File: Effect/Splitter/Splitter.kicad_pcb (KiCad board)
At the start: 2 copper layers, 32 x 68.5 mm, 9 parts, among them J1 Conn_01x04_Pin, J2 AudioJack2_Ground, J3 Conn_01x03_Pin, U1 OPA1655

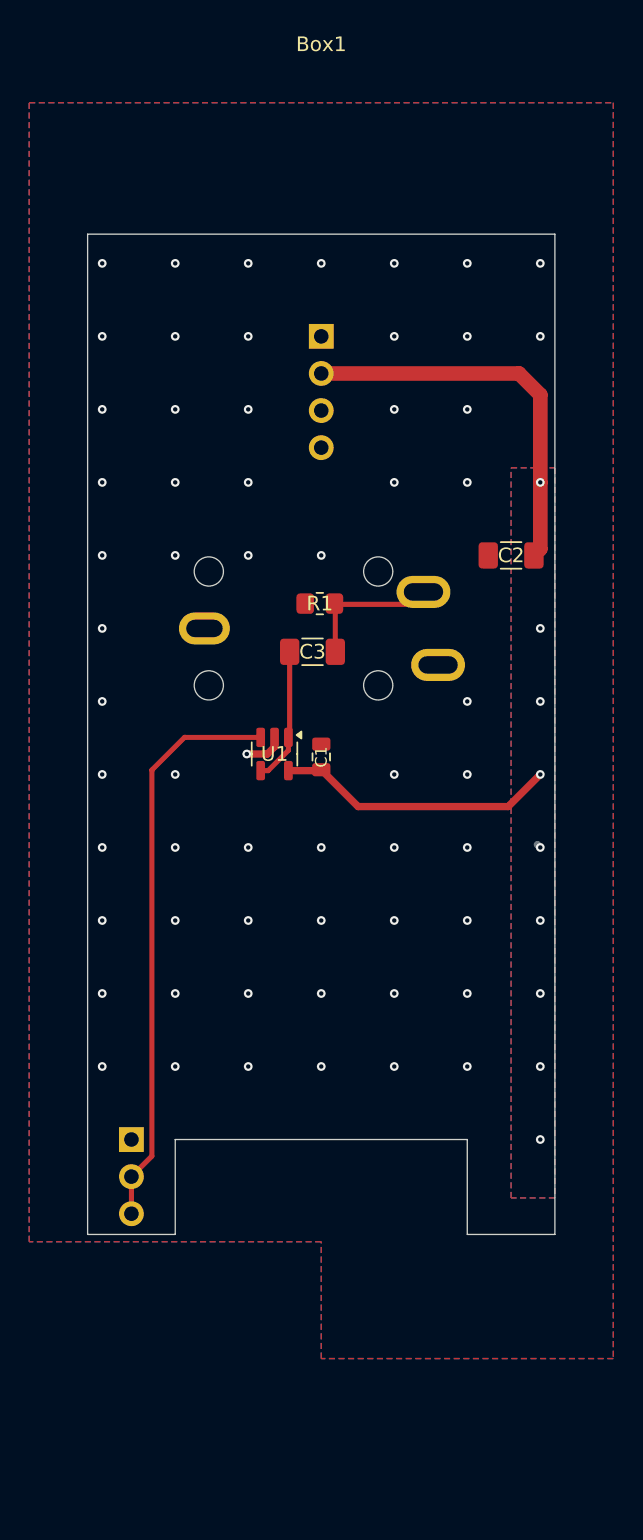
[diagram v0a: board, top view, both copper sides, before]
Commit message: Add volume control to 'splitter' board
Also stop being silly: this board needs no active circuitry.  The
incoming signal already comes from an op amp buffer on the base board,
there's no need to add a second one.

So remove the pointless op-amp, and replace the 100k resistor to ground
that is part of the signal rebiasing with a potentiometer for volume
control.

Signed-off-by: Linus Torvalds <torvalds@linux-foundation.org>
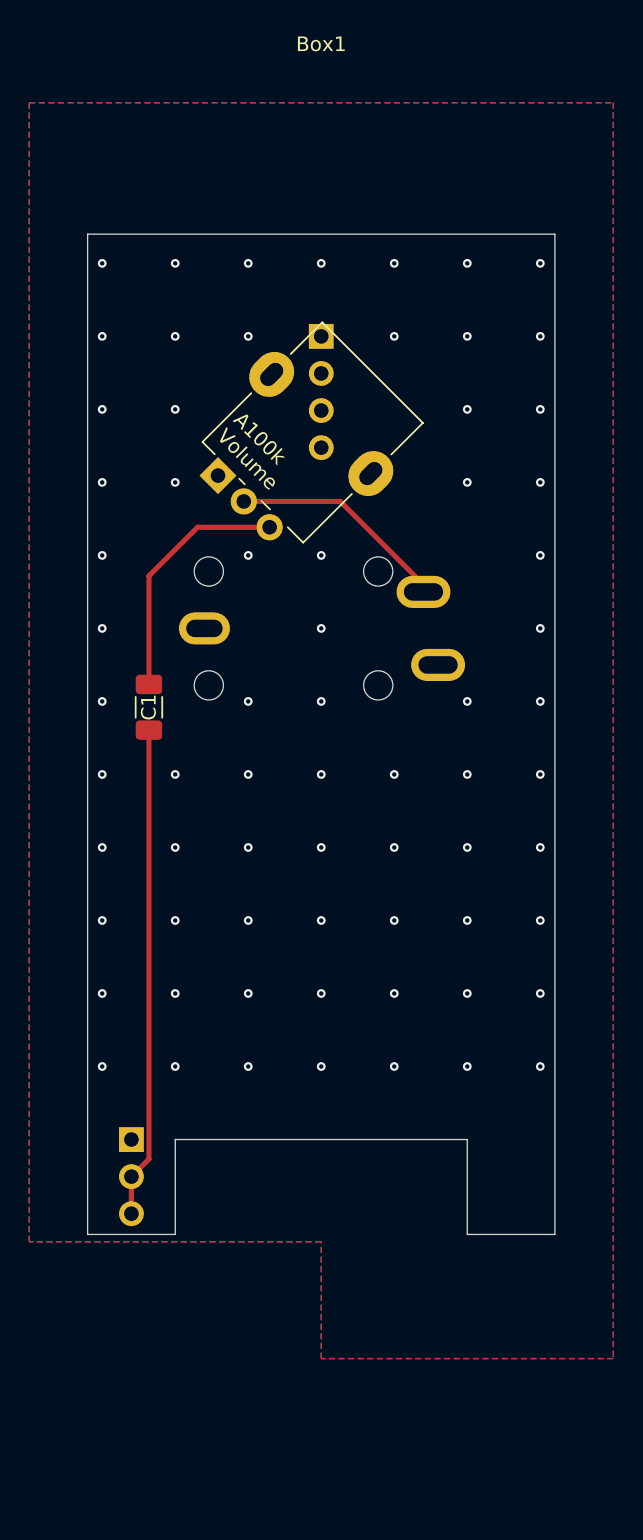
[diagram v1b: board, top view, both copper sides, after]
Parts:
- removed the C1 at (100.0, 98.8)
- removed C2: 22uF, Capacitor_SMD:C_1206_3216Metric_Pad1.33x1.80mm_HandSolder
- removed R1: 100k, Resistor_SMD:R_0805_2012Metric_Pad1.20x1.40mm_HandSolder
- removed U1: OPA1655, Package_TO_SOT_SMD:SOT-23-5
- added RV1: A100k Volume, Mylib:Potentiometer_9mm_MP, F.Cu at (100.0, 76.0)
- moved C1 11.8 mm to (88.2, 95.4), turned to -90 degrees
- renumbered C3 to C1
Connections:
- C1 pad 1: OUT^{RAW} -> Net-(C1-Pad1)
- C1 pad 2: Net-(U1--) -> IN
- J1 pad 2: +V -> unconnected-(J1-Pin_2-Pad2)
- J1 pad 3: GNDREF -> unconnected-(J1-Pin_3-Pad3)
- J2 pad T: OUT^{RAW} -> OUT
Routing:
- net +V: track 46.2 -> 0.00 mm, vias 9 -> 0
- net Net-(C1-Pad1): track 0.00 -> 17.1 mm
- net OUT: track 0.00 -> 15.2 mm
- net Net-(U1--): track 8.82 -> 0.00 mm
- net OUT^{RAW}: track 8.44 -> 0.00 mm
- net IN: track 39.3 -> 33.6 mm
- net GND: track 2.75 -> 0.00 mm, vias 59 -> 68
- removed copper zone on B.Cu, net +V
- removed copper zone on F.Cu, net +V
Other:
- board text added: "A100k Volume"
